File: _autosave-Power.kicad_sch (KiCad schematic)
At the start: 24 parts, among them U2 LD1117S33TR_SOT223, U3 LM2675M-5.0/NOPB

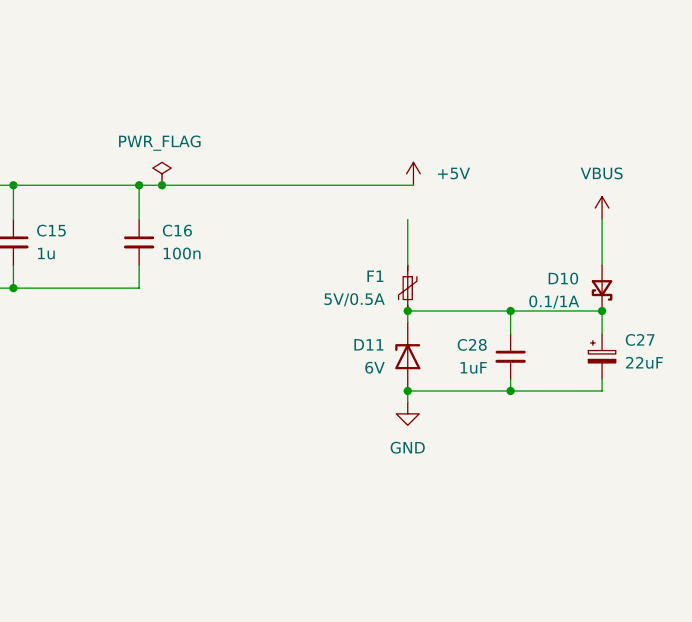
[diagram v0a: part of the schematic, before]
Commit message: Finished schematic
Added UCB C connection
Added CAN
Power ICs schematic fixed
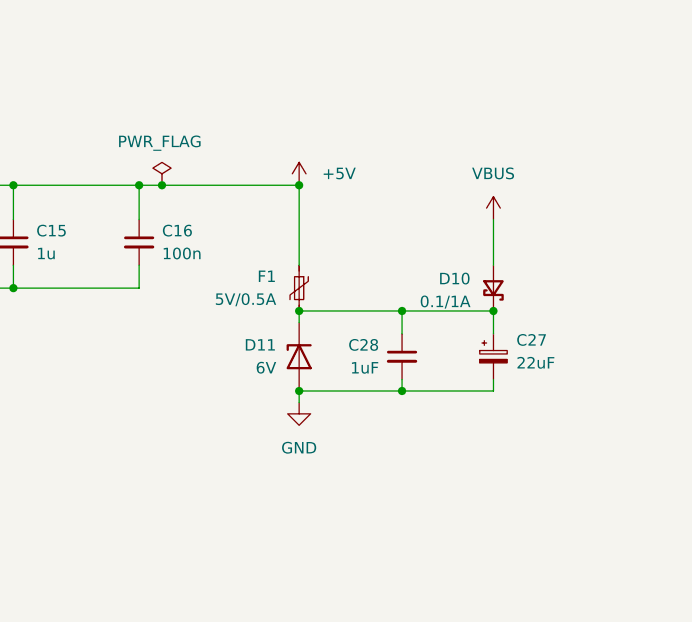
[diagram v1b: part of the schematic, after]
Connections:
- net +5V: now also F1.1
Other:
- moved on the sheet: C27, C28, D10, D11, F1
